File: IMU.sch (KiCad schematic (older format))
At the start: 8 parts, among them U3 BNO055

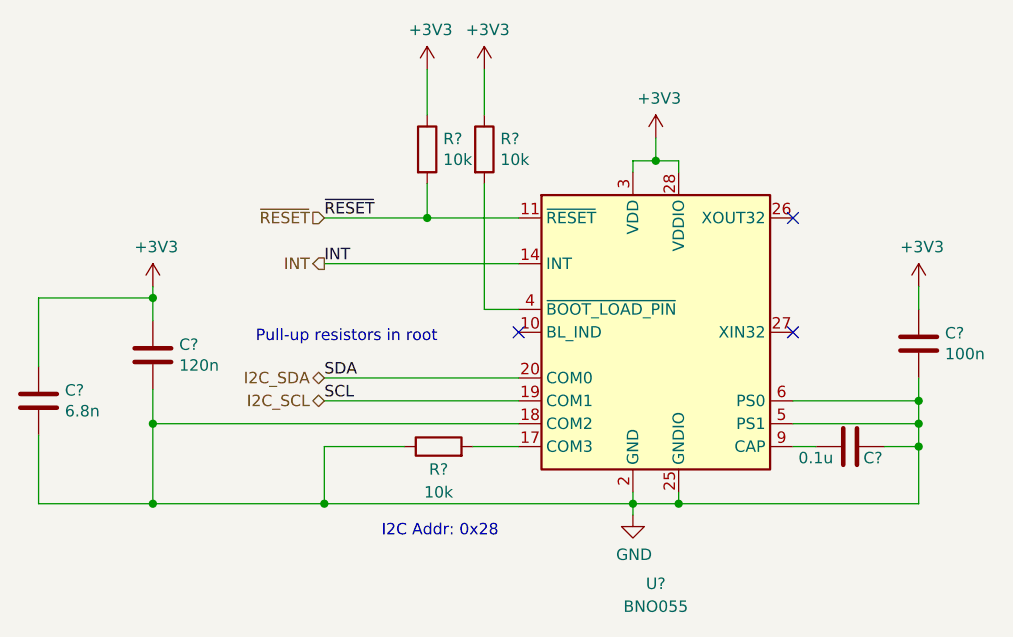
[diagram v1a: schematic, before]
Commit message: Initial layout of the Telemtry board.
The ethernet interface needs more work.
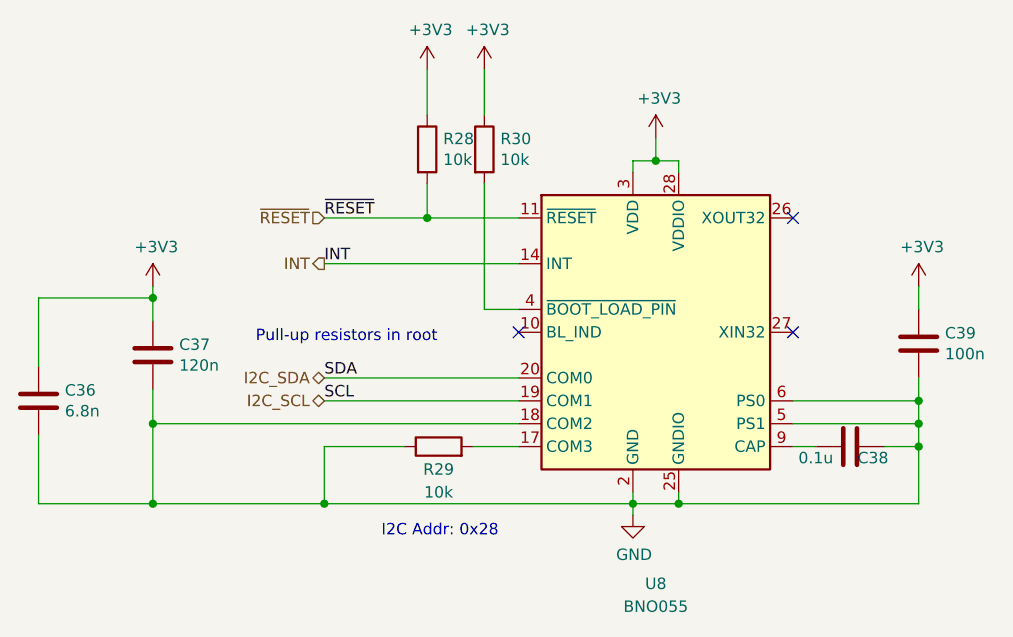
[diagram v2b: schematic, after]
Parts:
- gave numbers to parts that had none: 7
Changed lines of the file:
@@
 AR Path="/5EF56CFF" Ref="U?"  Part="1"
 AR Path="/5EF43BAC/5EF56CFF" Ref="U3"  Part="1"
-AR Path="/5F6DD18A/5EF56CFF" Ref="U?"  Part="1"
-F 0 "U?" H 6300 2700 50  0000 C CNN
+AR Path="/5F6DD18A/5EF56CFF" Ref="U8"  Part="1"
+F 0 "U8" H 6300 2700 50  0000 C CNN
 F 1 "BNO055" H 6300 2600 50  0000 C CNN
 F 2 "Package_LGA:LGA-28_5.2x3.8mm_P0.5mm" H 6550 3150 50  0001 L CNN
@@
 $EndComp
 $Comp
-L power:GND #PWR?
+L power:GND #PWR0160
 U 1 1 5EF56D05
 P 6200 4600
-F 0 "#PWR?" H 6200 4350 50  0001 C CNN
+F 0 "#PWR0160" H 6200 4350 50  0001 C CNN
 F 1 "GND" H 6205 4427 50  0000 C CNN
 F 2 "" H 6200 4600 50  0001 C CNN
@@
 	6200 4500 6200 4550
 $Comp
-L Device:C C?
+L Device:C C38
 U 1 1 5EF56D0E
 P 7150 4300
-F 0 "C?" V 7200 4400 50  0000 C CNN
+F 0 "C38" V 7200 4400 50  0000 C CNN
 F 1 "0.1u" V 7200 4150 50  0000 C CNN
 F 2 "Capacitor_SMD:C_0805_2012Metric" H 7188 4150 50  0001 C CNN
@@
 Connection ~ 7450 4200
 $Comp
-L Device:R R?
+L Device:R R28
 U 1 1 5EF56D1E
 P 5300 3000
-F 0 "R?" H 5370 3046 50  0000 L CNN
+F 0 "R28" H 5370 3046 50  0000 L CNN
 F 1 "10k" H 5370 2955 50  0000 L CNN
 F 2 "Resistor_SMD:R_0805_2012Metric" V 5230 3000 50  0001 C CNN
@@
 $EndComp
 $Comp
-L Device:C C?
+L Device:C C37
 U 1 1 5EF56D2A
 P 4100 3900
-F 0 "C?" H 4215 3946 50  0000 L CNN
+F 0 "C37" H 4215 3946 50  0000 L CNN
 F 1 "120n" H 4215 3855 50  0000 L CNN
 F 2 "Capacitor_SMD:C_0805_2012Metric" H 4138 3750 50  0001 C CNN
@@
 $EndComp
 $Comp
-L Device:C C?
+L Device:C C39
 U 1 1 5EF56D56
 P 7450 3850
-F 0 "C?" H 7565 3896 50  0000 L CNN
+F 0 "C39" H 7565 3896 50  0000 L CNN
 F 1 "100n" H 7565 3805 50  0000 L CNN
 F 2 "Capacitor_SMD:C_0805_2012Metric" H 7488 3700 50  0001 C CNN
@@
 	7450 4100 7450 4200
 $Comp
-L Device:R R?
+L Device:R R30
 U 1 1 5EF56D5F
 P 5550 3000
-F 0 "R?" H 5620 3046 50  0000 L CNN
+F 0 "R30" H 5620 3046 50  0000 L CNN
 F 1 "10k" H 5620 2955 50  0000 L CNN
 F 2 "Resistor_SMD:R_0805_2012Metric" V 5480 3000 50  0001 C CNN
@@
 NoConn ~ 5700 3800
 $Comp
-L Device:R R?
+L Device:R R29
 U 1 1 5EFC1422
 P 5350 4300
-F 0 "R?" V 5250 4300 50  0000 C CNN
+F 0 "R29" V 5250 4300 50  0000 C CNN
 F 1 "10k" V 5150 4300 50  0000 C CNN
 F 2 "Resistor_SMD:R_0805_2012Metric" V 5280 4300 50  0001 C CNN
@@
 	6300 2950 6300 3050
 $Comp
-L power:+3V3 #PWR?
+L power:+3V3 #PWR0161
 U 1 1 5F16055B
 P 6300 2950
-F 0 "#PWR?" H 6300 2800 50  0001 C CNN
+F 0 "#PWR0161" H 6300 2800 50  0001 C CNN
 F 1 "+3V3" H 6315 3123 50  0000 C CNN
 F 2 "" H 6300 2950 50  0001 C CNN
@@
 $EndComp
 $Comp
-L power:+3V3 #PWR?
+L power:+3V3 #PWR0162
 U 1 1 5F1606C7
 P 7450 3600
-F 0 "#PWR?" H 7450 3450 50  0001 C CNN
+F 0 "#PWR0162" H 7450 3450 50  0001 C CNN
 F 1 "+3V3" H 7465 3773 50  0000 C CNN
 F 2 "" H 7450 3600 50  0001 C CNN
@@
 $EndComp
 $Comp
-L power:+3V3 #PWR?
+L power:+3V3 #PWR0163
 U 1 1 5F16088A
 P 5550 2650
-F 0 "#PWR?" H 5550 2500 50  0001 C CNN
+F 0 "#PWR0163" H 5550 2500 50  0001 C CNN
 F 1 "+3V3" H 5565 2823 50  0000 C CNN
 F 2 "" H 5550 2650 50  0001 C CNN
@@
 $EndComp
 $Comp
-L power:+3V3 #PWR?
+L power:+3V3 #PWR0164
 U 1 1 5F160A1A
 P 5300 2650
-F 0 "#PWR?" H 5300 2500 50  0001 C CNN
+F 0 "#PWR0164" H 5300 2500 50  0001 C CNN
 F 1 "+3V3" H 5315 2823 50  0000 C CNN
 F 2 "" H 5300 2650 50  0001 C CNN
@@
 $EndComp
 $Comp
-L power:+3V3 #PWR?
+L power:+3V3 #PWR0165
 U 1 1 5F160BBC
 P 4100 3600
-F 0 "#PWR?" H 4100 3450 50  0001 C CNN
+F 0 "#PWR0165" H 4100 3450 50  0001 C CNN
 F 1 "+3V3" H 4115 3773 50  0000 C CNN
 F 2 "" H 4100 3600 50  0001 C CNN
@@
 I2C Addr: 0x28
 $Comp
-L Device:C C?
+L Device:C C36
 U 1 1 5F6FCE6A
 P 3600 4100
-F 0 "C?" H 3715 4146 50  0000 L CNN
+F 0 "C36" H 3715 4146 50  0000 L CNN
 F 1 "6.8n" H 3715 4055 50  0000 L CNN
 F 2 "Capacitor_SMD:C_0805_2012Metric" H 3638 3950 50  0001 C CNN

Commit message: Lay out the Telemetry board.
This is the initial draft of the Telemetry board layout. A few
debugging pins changed (on the SD card) for easier routing.

There is still some uncertainty with regard to the routing of the
Ethernet traces. According to my calculations, the differential
impedence between the RX+/- traces and the TX+/- traces is around
150R, which is 50% higher than one source was recommending. I am
uncertain how to reduce this though, and I am unclear as to how
much this will affect performance, especially when the traces
cover such a short distance.
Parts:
- U3: symbol Sensor_Motion:BNO055 -> Telemetry-Primary-rescue:BNO055-Sensor_Motion
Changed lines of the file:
@@
 $EndDescr
 $Comp
-L Sensor_Motion:BNO055 U?
+L Telemetry-Primary-rescue:BNO055-Sensor_Motion U?
 U 1 1 5EF56CFF
 P 6300 3800
